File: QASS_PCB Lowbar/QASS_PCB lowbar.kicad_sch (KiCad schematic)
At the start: 81 parts, among them J1 Conn_01x02_Pin, J2 Conn_01x05_Pin, J3 Conn_01x05_Pin, J4 Conn_01x02_Pin, J5 Conn_01x05_Pin, J6 Conn_01x05_Pin

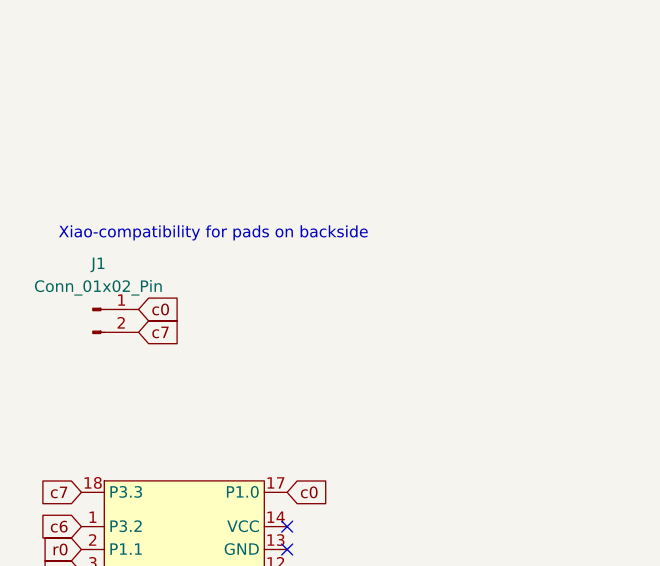
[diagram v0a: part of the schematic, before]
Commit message: v1.1 - [x] Beschriftung der Switches in der BottomRow auf Oberem PCB - [x] Doppelten 6+3u stab entfert - [x] Switchpositionen auf unterem PCB auch markiert - [x] Unteren zwei Löcher für MCU weggelassen, weil wird nicht gebraucht - [x] Added "MCU on this side" and reference to Xiao (sadly not compatible)
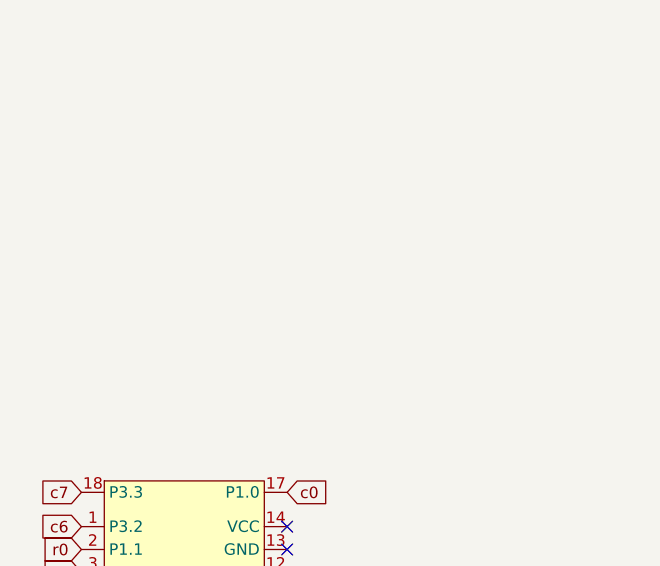
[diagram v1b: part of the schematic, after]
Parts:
- removed J1: Conn_01x02_Pin, Connector_PinHeader_2.54mm:PinHeader_1x02_P2.54mm_Vertical, symbol Connector:Conn_01x02_Pin
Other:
- note removed: "Xiao-compatibility for pads on backside"
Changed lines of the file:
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@@
 		)
 	)
-	(text "Xiao-compatibility for pads on backside"
-		(exclude_from_sim no)
-		(at 26.67 43.18 0)
-		(effects
-			(font
-				(size 1.27 1.27)
-			)
-			(justify left bottom)
-		)
-	)
 	(text "Spacebars 3u"
 		(exclude_from_sim no)
@@
 		)
 	)
-	(global_label "c0"
-		(shape input)
-		(at 35.56 50.8 0)
-		(fields_autoplaced yes)
-		(effects
-			(font
-				(size 1.27 1.27)
-			)
-			(justify left)
-		)
-		(property "Intersheetrefs" "${INTERSHEET_REFS}"
-			(at 40.8433 50.8 0)
-			(effects
-				(font
-					(size 1.27 1.27)
-				)
-				(justify left)
-				(hide yes)
-			)
-		)
-	)
 	(global_label "c2"
 		(shape input)
@@
 		)
 	)
-	(global_label "c7"
-		(shape input)
-		(at 35.56 53.34 0)
-		(fields_autoplaced yes)
-		(effects
-			(font
-				(size 1.27 1.27)
-			)
-			(justify left)
-		)
-		(property "Intersheetrefs" "${INTERSHEET_REFS}"
-			(at 40.8433 53.34 0)
-			(effects
-				(font
-					(size 1.27 1.27)
-				)
-				(justify left)
-				(hide yes)
-			)
-		)
-	)
 	(global_label "c4"
 		(shape input)
@@
 					(unit 1)
 				)
-			)
-		)
-	)
-	(symbol
-		(lib_id "Connector:Conn_01x02_Pin")
-		(at 30.48 50.8 0)
-		(unit 1)
-		(exclude_from_sim no)
-		(in_bom yes)
-		(on_board yes)
-		(dnp no)
-		(fields_autoplaced yes)
-		(property "Reference" "J1"
-			(at 31.115 45.72 0)
-			(effects
-				(font
-					(size 1.27 1.27)
-				)
-			)
-		)
-		(property "Value" "Conn_01x02_Pin"
-			(at 31.115 48.26 0)
-			(effects
-				(font
-					(size 1.27 1.27)
-				)
-			)
-		)
-		(property "Footprint" "Connector_PinHeader_2.54mm:PinHeader_1x02_P2.54mm_Vertical"
-			(at 30.48 50.8 0)
-			(effects
-				(font
-					(size 1.27 1.27)
-				)
-				(hide yes)
-			)
-		)
-		(property "Datasheet" "~"
-			(at 30.48 50.8 0)
-			(effects
-				(font
-					(size 1.27 1.27)
-				)
-				(hide yes)
-			)
-		)
-		(property "Description" ""
-			(at 30.48 50.8 0)
-			(effects
-				(font
-					(size 1.27 1.27)
-				)
-				(hide yes)
-			)
-		)
-		(pin "1"
-		)
-		(pin "2"
-		)
-		(instances
-			(project "QASS_PCB lowbar"
-				(path "/4e836cba-8d9e-4ad4-ae4d-2f7aa930d50f"
-					(reference "J1")
-					(unit 1)
-				)
